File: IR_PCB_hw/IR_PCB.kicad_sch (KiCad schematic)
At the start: 130 parts, among them Q1 M28S, Q10 SI2301, Q11 SI2301, Q2 M28S, Q3 TSOP4856, Q4 TSOP4856, Q5 SI2301, Q6 TSOP4856, Q7 SI2301, Q8 SI2301, Q9 SI2301

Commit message: Replace USB conn with micro one Replace 0402 wit 0603
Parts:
- removed R2, R3: 5k1, Resistors:RES_0402_Fab, symbol Tittar_kl:R
- removed XL4: USB_C 24PF-009, Connectors:USBC_24PF-009, symbol Connectors_kl:USB_C
- added XL4: DS1105-11, Connectors:USBmicro_Connfly_DS1105-11, symbol Connectors_kl:USB_MICRO_3H
- C10: footprint Capacitors:CAP_0603_Fab -> Capacitors:CAP_0603_Silks
- C11: renamed from C12; footprint Capacitors:CAP_0402_Fab -> Capacitors:CAP_0603_Silks
- C12: renamed from C13; footprint Capacitors:CAP_0402_Fab -> Capacitors:CAP_0603_Silks
- C13: renamed from C14; footprint Capacitors:CAP_0402_Fab -> Capacitors:CAP_0603_Silks
- C14: renamed from C11; footprint Capacitors:CAP_0402_Fab -> Capacitors:CAP_0603_Silks
- C15: renamed from C16; footprint Capacitors:CAP_0402_Fab -> Capacitors:CAP_0603_Silks
- C17: renamed from C18; footprint Capacitors:CAP_0402_Fab -> Capacitors:CAP_0603_Silks
- C19: renamed from C20; footprint Capacitors:CAP_0402_Fab -> Capacitors:CAP_0603_Silks
- C2, C3, C4, C5, C6, C7, C8, C9: footprint Capacitors:CAP_0402_Fab -> Capacitors:CAP_0603_Silks
- C21: renamed from C22; footprint Capacitors:CAP_0402_Fab -> Capacitors:CAP_0603_Silks
- C22: renamed from C23; footprint Capacitors:CAP_0603_Fab -> Capacitors:CAP_0603_Silks
- C23: renamed from C24; footprint Capacitors:CAP_0402_Fab -> Capacitors:CAP_0603_Silks
- C24: renamed from C25; footprint Capacitors:CAP_0603_Fab -> Capacitors:CAP_0603_Silks
- C25: renamed from C26; footprint Capacitors:CAP_0603_Fab -> Capacitors:CAP_0603_Silks
- D9: renamed from D13; Price 10.59 -> 10.35
- R1: footprint Resistors:RES_0402_Fab -> Resistors:RES_0603_Silks
- R10: renamed from R12; footprint Resistors:RES_0402_Fab -> Resistors:RES_0603_Silks
- R11: renamed from R13; footprint Resistors:RES_0402_Fab -> Resistors:RES_0603_Silks
- R12: renamed from R14; footprint Resistors:RES_0402_Fab -> Resistors:RES_0603_Silks
- R13: renamed from R15; footprint Resistors:RES_0402_Fab -> Resistors:RES_0603_Silks
- R14: renamed from R16; footprint Resistors:RES_0402_Fab -> Resistors:RES_0603_Silks
- R15: renamed from R17; footprint Resistors:RES_0402_Fab -> Resistors:RES_0603_Silks
- R16: renamed from R18; footprint Resistors:RES_0402_Fab -> Resistors:RES_0603_Silks
- R17: renamed from R19; footprint Resistors:RES_0402_Fab -> Resistors:RES_0603_Silks
- R18: renamed from R20; footprint Resistors:RES_0402_Fab -> Resistors:RES_0603_Silks
- R19: renamed from R21; footprint Resistors:RES_0402_Fab -> Resistors:RES_0603_Silks
- R2: renamed from R4; footprint Resistors:RES_0402_Fab -> Resistors:RES_0603_Silks
- R20: renamed from R22; footprint Resistors:RES_0402_Fab -> Resistors:RES_0603_Silks
- R21: renamed from R23; footprint Resistors:RES_0402_Fab -> Resistors:RES_0603_Silks
- R22: renamed from R24; footprint Resistors:RES_0402_Fab -> Resistors:RES_0603_Silks
- R23: renamed from R29; footprint Resistors:RES_0402_Fab -> Resistors:RES_0603_Silks
- R24: renamed from R25; footprint Resistors:RES_0402_Fab -> Resistors:RES_0603_Silks
- R25: renamed from R26; footprint Resistors:RES_0402_Fab -> Resistors:RES_0603_Silks
- R26: renamed from R27; footprint Resistors:RES_0402_Fab -> Resistors:RES_0603_Silks
- R3: renamed from R5; footprint Resistors:RES_0402_Fab -> Resistors:RES_0603_Silks
- R4: renamed from R6; footprint Resistors:RES_0402_Fab -> Resistors:RES_0603_Silks
- R5: renamed from R7; footprint Resistors:RES_0402_Fab -> Resistors:RES_0603_Silks
- R6: renamed from R8; footprint Resistors:RES_0402_Fab -> Resistors:RES_0603_Silks
- R7: renamed from R9; footprint Resistors:RES_0402_Fab -> Resistors:RES_0603_Silks
- R8: renamed from R10; footprint Resistors:RES_0402_Fab -> Resistors:RES_0603_Silks
- R9: renamed from R11; footprint Resistors:RES_0402_Fab -> Resistors:RES_0603_Silks
- renumbered C17 to C16, C19 to C18, C21 to C20, D9 to D10, D10 to D11, D11 to D12, D12 to D13, Q9 to Q10, Q10 to Q9, TP2 to TP1, TP3 to TP2, TP4 to TP3, TP5 to TP4, XL14 to XL10, XL15 to XL11, XL16 to XL12, XL17 to XL13, XL18 to XL14, XL19 to XL15, XL20 to XL16, XL21 to XL17, XL22 to XL18, XL23 to XL19, XL24 to XL20, XL7 to XL6, XL8 to XL7, XL9 to XL8, XL10 to XL9
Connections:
- net +5vUSB: now also XL4.1 (UVcc)
- net GND: now also XL4.4 (UID), XL4.5 (UGND)
- net USB_D+: now also XL4.3 (D+)
- net USB_D-: now also XL4.2 (D-)
- no-connect marks 18 -> 7

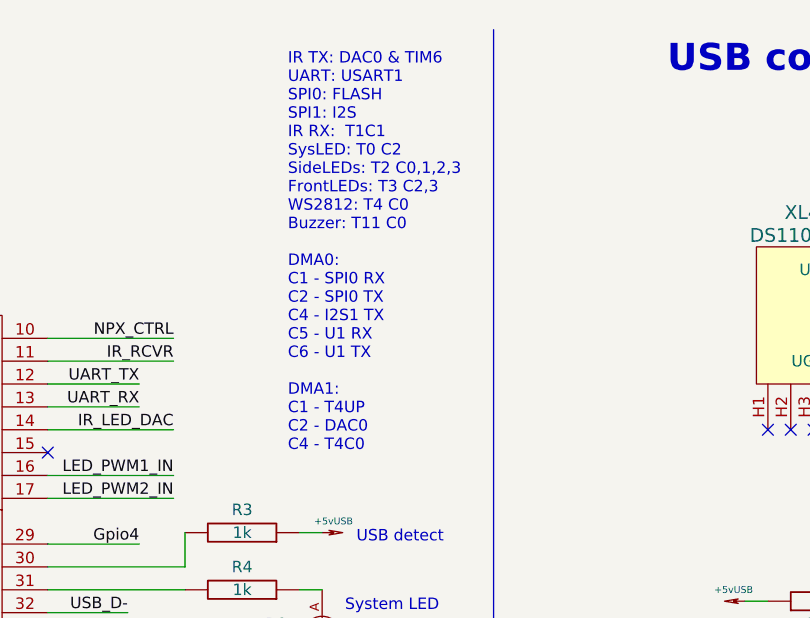
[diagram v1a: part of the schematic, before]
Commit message: Switching to CDC+MSD
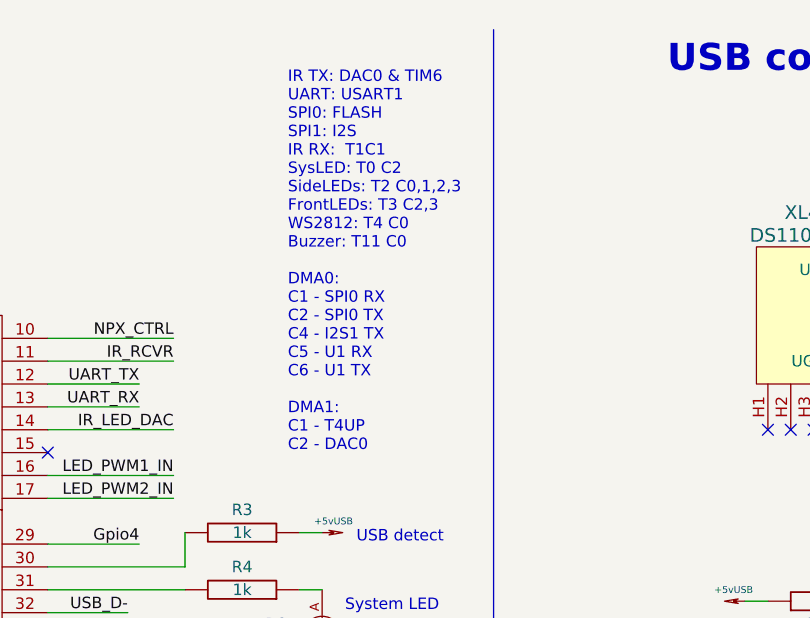
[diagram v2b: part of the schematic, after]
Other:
- note added: "IR TX: DAC0 & TIM6 UART: USART1 SPI0: FLASH SPI1: I2S IR RX: T1C1 SysLED: T0 C2 SideLEDs: T2 C0,1,2,3 FrontLEDs: T3 C2,3 WS2812: T4 C0 Buzzer: T11 C0 DMA0: C1 - SPI0 RX C2 - SPI0 TX C4 - I2S1 TX C5 - U1 RX C6 - U1 TX DMA1: C1 - T4UP C2 - DAC0"
- note removed: "IR TX: DAC0 & TIM6 UART: USART1 SPI0: FLASH SPI1: I2S IR RX: T1C1 SysLED: T0 C2 SideLEDs: T2 C0,1,2,3 FrontLEDs: T3 C2,3 WS2812: T4 C0 Buzzer: T11 C0 DMA0: C1 - SPI0 RX C2 - SPI0 TX C4 - I2S1 TX C5 - U1 RX C6 - U1 TX DMA1: C1 - T4UP C2 - DAC0 C4 - T4C0"
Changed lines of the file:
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@@
     (effects (font (size 1.27 1.27) bold) (justify left bottom))
   )
-  (text "IR TX: DAC0 & TIM6\nUART: USART1\nSPI0: FLASH\nSPI1: I2S\nIR RX:  T1C1\nSysLED: T0 C2\nSideLEDs: T2 C0,1,2,3\nFrontLEDs: T3 C2,3\nWS2812: T4 C0\nBuzzer: T11 C0\n\nDMA0:\nC1 - SPI0 RX\nC2 - SPI0 TX\nC4 - I2S1 TX\nC5 - U1 RX\nC6 - U1 TX\n\nDMA1:\nC1 - T4UP\nC2 - DAC0\nC4 - T4C0"
+  (text "IR TX: DAC0 & TIM6\nUART: USART1\nSPI0: FLASH\nSPI1: I2S\nIR RX:  T1C1\nSysLED: T0 C2\nSideLEDs: T2 C0,1,2,3\nFrontLEDs: T3 C2,3\nWS2812: T4 C0\nBuzzer: T11 C0\n\nDMA0:\nC1 - SPI0 RX\nC2 - SPI0 TX\nC4 - I2S1 TX\nC5 - U1 RX\nC6 - U1 TX\n\nDMA1:\nC1 - T4UP\nC2 - DAC0"
     (at 167.64 60.96 0)
     (effects (font (size 1.27 1.27)) (justify left bottom))

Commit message: Preparation for factory
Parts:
- BZ1, D1, D10, D11, D12, D13, D3, D4, D5, D6, D7, D8, Q3, Q4, Q6: Comment (none) -> DoNotMount
- C10: PN CL10A106MP8NNNC -> CL10A106MQ8NNNC; URL https://www.promelec.ru/product/335887/ -> https://www.promelec.ru/product/334535/; Voltage 10v -> 6V3
- C2: PN CC0402KRX7R7BB104 -> CC0603KRX7R9BB104; Price 0.17 -> 0.34; URL https://www.promelec.ru/product/141827/ -> https://www.promelec.ru/product/126354/; Voltage 16V -> 50V
- C3: Manufacturer Murata -> Samsung; PN GRM155R61A225KE95D -> CL10A225KO8NNNC; URL https://www.promelec.ru/product/315859/ -> https://www.promelec.ru/product/316243/; Voltage 10V -> 16V
- C4: PN CC0402JRNPO9BN180 -> CC0603JRNPO9BN180; URL https://www.promelec.ru/product/188454/ -> https://www.promelec.ru/product/128216/
- C6: Manufacturer Hottech -> Samsung; PN C1005A105K100NT -> CL10A105KO8NNNC; URL https://www.promelec.ru/product/522035/ -> https://www.promelec.ru/product/335757/; Voltage 10V -> 16V
- R1: PN RC0402FR-0710KL -> RC0603FR-0710KL; URL https://www.promelec.ru/product/305624/ -> https://www.promelec.ru/product/108599/
- R2: PN RI0402L1001FT -> RC0603FR-071KL; URL https://www.promelec.ru/product/415937/ -> https://www.promelec.ru/product/22771/
- R5: PN RI0402L2R00FT -> RC0603FR-072RL; URL https://www.promelec.ru/product/529480/ -> https://www.promelec.ru/product/59444/
- R6: PN RC0402FR-07100RL -> RC0603FR-07100RL; URL https://www.promelec.ru/product/229700/ -> https://www.promelec.ru/product/57782/
- R9: PN RC0402FR-0751RL -> RC0603FR-0751RL; URL https://www.promelec.ru/product/305769/ -> https://www.promelec.ru/product/18324/
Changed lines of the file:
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@@
       (effects (font (size 2.0066 2.0066)) hide)
     )
-    (property "PN" "RC0402FR-0751RL" (at 391.16 142.24 0)
+    (property "PN" "RC0603FR-0751RL" (at 391.16 142.24 0)
       (effects (font (size 1.27 1.27)) hide)
     )
@@
       (effects (font (size 1.27 1.27)) hide)
     )
-    (property "URL" "https://www.promelec.ru/product/305769/" (at 391.16 142.24 90)
+    (property "URL" "https://www.promelec.ru/product/18324/" (at 391.16 142.24 90)
       (effects (font (size 1.27 1.27)) hide)
     )
@@
       (effects (font (size 1.27 1.27)) hide)
     )
+    (property "Comment" "DoNotMount" (at 389.89 34.29 90)
+      (effects (font (size 1.27 1.27)) hide)
+    )
     (pin "A")
     (pin "C")
@@
       (effects (font (size 1.27 1.27)) hide)
     )
-    (property "PN" "C1005A105K100NT" (at 245.11 118.11 0)
+    (property "PN" "CL10A105KO8NNNC" (at 245.11 118.11 0)
       (effects (font (size 1.27 1.27)) hide)
     )
-    (property "Manufacturer" "Hottech" (at 245.11 118.11 0)
+    (property "Manufacturer" "Samsung" (at 245.11 118.11 0)
       (effects (font (size 1.27 1.27)) hide)
     )
@@
       (effects (font (size 1.27 1.27)) hide)
     )
-    (property "Voltage" "10V" (at 245.11 118.11 0)
+    (property "Voltage" "16V" (at 245.11 118.11 0)
       (effects (font (size 1.27 1.27)) (justify left))
     )
-    (property "URL" "https://www.promelec.ru/product/522035/" (at 245.11 118.11 0)
+    (property "URL" "https://www.promelec.ru/product/335757/" (at 245.11 118.11 0)
       (effects (font (size 1.27 1.27)) hide)
     )
@@
       (effects (font (size 1.27 1.27)) hide)
     )
+    (property "Comment" "DoNotMount" (at 400.05 85.09 90)
+      (effects (font (size 1.27 1.27)) hide)
+    )
     (pin "A")
     (pin "C")
@@
       (effects (font (size 1.27 1.27)) hide)
     )
+    (property "Comment" "DoNotMount" (at 316.23 153.67 0)
+      (effects (font (size 1.27 1.27)) hide)
+    )
     (pin "1")
     (pin "2")
@@
       (effects (font (size 1.27 1.27)) hide)
     )
+    (property "Comment" "DoNotMount" (at 238.76 254 0)
+      (effects (font (size 1.27 1.27)) hide)
+    )
     (pin "A")
     (pin "C")
@@
       (effects (font (size 1.27 1.27)) hide)
     )
+    (property "Comment" "DoNotMount" (at 238.76 226.06 0)
+      (effects (font (size 1.27 1.27)) hide)
+    )
     (pin "A")
     (pin "C")
@@
       (effects (font (size 1.27 1.27)) hide)
     )
+    (property "Comment" "DoNotMount" (at 238.76 262.89 0)
+      (effects (font (size 1.27 1.27)) hide)
+    )
     (pin "A")
     (pin "C")
@@
       (effects (font (size 1.27 1.27)) hide)
     )
+    (property "Comment" "DoNotMount" (at 397.51 236.22 0)
+      (effects (font (size 1.27 1.27)) hide)
+    )
     (pin "1")
     (pin "2")
@@
       (effects (font (size 2.0066 2.0066)) hide)
     )
-    (property "PN" "RC0402FR-07100RL" (at 393.7 77.47 0)
+    (property "PN" "RC0603FR-07100RL" (at 393.7 77.47 0)
       (effects (font (size 1.27 1.27)) hide)
     )
@@
       (effects (font (size 1.27 1.27)) hide)
     )
-    (property "URL" "https://www.promelec.ru/product/229700/" (at 393.7 77.47 90)
+    (property "URL" "https://www.promelec.ru/product/57782/" (at 393.7 77.47 90)
       (effects (font (size 1.27 1.27)) hide)
     )
@@
       (effects (font (size 1.27 1.27)) hide)
     )
-    (property "PN" "GRM155R61A225KE95D" (at 238.76 77.47 0)
+    (property "PN" "CL10A225KO8NNNC" (at 238.76 77.47 0)
       (effects (font (size 1.27 1.27)) hide)
     )
-    (property "Manufacturer" "Murata" (at 238.76 77.47 0)
+    (property "Manufacturer" "Samsung" (at 238.76 77.47 0)
       (effects (font (size 1.27 1.27)) hide)
     )
@@
       (effects (font (size 1.27 1.27)) hide)
     )
-    (property "Voltage" "10V" (at 238.76 78.74 0)
+    (property "Voltage" "16V" (at 238.76 78.74 0)
       (effects (font (size 0.7 0.7)) (justify left))
     )
-    (property "URL" "https://www.promelec.ru/product/315859/" (at 238.76 77.47 90)
+    (property "URL" "https://www.promelec.ru/product/316243/" (at 238.76 77.47 90)
       (effects (font (size 1.27 1.27)) hide)
     )
@@
       (effects (font (size 1.27 1.27)) hide)
     )
+    (property "Comment" "DoNotMount" (at 238.76 234.95 0)
+      (effects (font (size 1.27 1.27)) hide)
+    )
     (pin "A")
     (pin "C")
@@
       (effects (font (size 1.27 1.27)) hide)
     )
+    (property "Comment" "DoNotMount" (at 364.49 138.43 0)
+      (effects (font (size 1.27 1.27)) hide)
+    )
     (pin "1")
     (pin "2")
@@
       (effects (font (size 2.0066 2.0066)) hide)
     )
-    (property "PN" "RI0402L1001FT" (at 326.39 64.77 0)
+    (property "PN" "RC0603FR-071KL" (at 326.39 64.77 0)
       (effects (font (size 1.27 1.27)) hide)
     )
@@
       (effects (font (size 1.27 1.27)) hide)
     )
-    (property "URL" "https://www.promelec.ru/product/415937/" (at 326.39 64.77 0)
+    (property "URL" "https://www.promelec.ru/product/22771/" (at 326.39 64.77 0)
       (effects (font (size 1.27 1.27)) hide)
     )
@@
       (effects (font (size 2.0066 2.0066)) hide)
     )
-    (property "PN" "RC0402FR-0710KL" (at 300.99 48.26 0)
+    (property "PN" "RC0603FR-0710KL" (at 300.99 48.26 0)
       (effects (font (size 1.27 1.27)) hide)
     )
@@
       (effects (font (size 1.27 1.27)) hide)
     )
-    (property "URL" "https://www.promelec.ru/product/305624/" (at 300.99 48.26 90)
+    (property "URL" "https://www.promelec.ru/product/108599/" (at 300.99 48.26 90)
       (effects (font (size 1.27 1.27)) hide)
     )
@@
       (effects (font (size 1.27 1.27)) hide)
     )
-    (property "PN" "CC0402JRNPO9BN180" (at 175.26 109.22 0)
+    (property "PN" "CC0603JRNPO9BN180" (at 175.26 109.22 0)
       (effects (font (size 1.27 1.27)) hide)
     )
@@
       (effects (font (size 1.27 1.27)) (justify left) hide)
     )
-    (property "URL" "https://www.promelec.ru/product/188454/" (at 175.26 109.22 90)
+    (property "URL" "https://www.promelec.ru/product/128216/" (at 175.26 109.22 90)
       (effects (font (size 1.27 1.27)) hide)
     )
@@
       (effects (font (size 1.524 1.524)) hide)
     )
-    (property "Price" "0.17" (at 317.5 34.29 0)
+    (property "Price" "0.34" (at 317.5 34.29 0)
       (effects (font (size 1.524 1.524)) hide)
     )
@@
       (effects (font (size 1.27 1.27)) hide)
     )
-    (property "PN" "CC0402KRX7R7BB104" (at 317.5 34.29 0)
+    (property "PN" "CC0603KRX7R9BB104" (at 317.5 34.29 0)
       (effects (font (size 1.27 1.27)) hide)
     )
@@
       (effects (font (size 1.27 1.27)) hide)
     )
-    (property "Voltage" "16V" (at 317.5 34.29 0)
+    (property "Voltage" "50V" (at 317.5 34.29 0)
       (effects (font (size 1.27 1.27)) (justify left))
     )
-    (property "URL" "https://www.promelec.ru/product/141827/" (at 317.5 34.29 0)
+    (property "URL" "https://www.promelec.ru/product/126354/" (at 317.5 34.29 0)
       (effects (font (size 1.27 1.27)) hide)
     )
@@
       (effects (font (size 1.27 1.27)) hide)
     )
+    (property "Comment" "DoNotMount" (at 238.76 189.23 0)
+      (effects (font (size 1.27 1.27)) hide)
+    )
     (pin "A")
     (pin "C")
@@
       (effects (font (size 1.27 1.27)) hide)
     )
+    (property "Comment" "DoNotMount" (at 238.76 198.12 0)
+      (effects (font (size 1.27 1.27)) hide)
+    )
     (pin "A")
     (pin "C")
@@
       (effects (font (size 1.27 1.27)) hide)
     )
+    (property "Comment" "DoNotMount" (at 364.49 166.37 0)
+      (effects (font (size 1.27 1.27)) hide)
+    )
     (pin "1")
     (pin "2")
@@
       (effects (font (size 1.27 1.27)) hide)
     )
+    (property "Comment" "DoNotMount" (at 238.76 161.29 0)
+      (effects (font (size 1.27 1.27)) hide)
+    )
     (pin "A")
     (pin "C")
@@
       (effects (font (size 1.27 1.27)) hide)
     )
+    (property "Comment" "DoNotMount" (at 238.76 170.18 0)
+      (effects (font (size 1.27 1.27)) hide)
+    )
     (pin "A")
     (pin "C")
@@
       (effects (font (size 1.27 1.27)) hide)
     )
-    (property "PN" "CL10A106MP8NNNC" (at 53.34 121.92 0)
+    (property "PN" "CL10A106MQ8NNNC" (at 53.34 121.92 0)
       (effects (font (size 1.27 1.27)) hide)
     )
@@
       (effects (font (size 1.27 1.27)) hide)
     )
-    (property "Voltage" "10v" (at 53.34 121.92 0)
+    (property "Voltage" "6V3" (at 53.34 121.92 0)
       (effects (font (size 1.27 1.27)) (justify left))
     )
-    (property "URL" "https://www.promelec.ru/product/335887/" (at 53.34 121.92 0)
+    (property "URL" "https://www.promelec.ru/product/334535/" (at 53.34 121.92 0)
       (effects (font (size 1.27 1.27)) hide)
     )
@@
       (effects (font (size 2.0066 2.0066)) hide)
     )
-    (property "PN" "RI0402L2R00FT" (at 227.33 77.47 0)
+    (property "PN" "RC0603FR-072RL" (at 227.33 77.47 0)
       (effects (font (size 1.27 1.27)) hide)
     )
@@
       (effects (font (size 1.27 1.27)) hide)
     )
-    (property "URL" "https://www.promelec.ru/product/529480/" (at 227.33 77.47 90)
+    (property "URL" "https://www.promelec.ru/product/59444/" (at 227.33 77.47 90)
       (effects (font (size 1.27 1.27)) hide)
     )
@@
       (effects (font (size 1.27 1.27)) hide)
     )
+    (property "Comment" "DoNotMount" (at 400.05 109.22 90)
+      (effects (font (size 1.27 1.27)) hide)
+    )

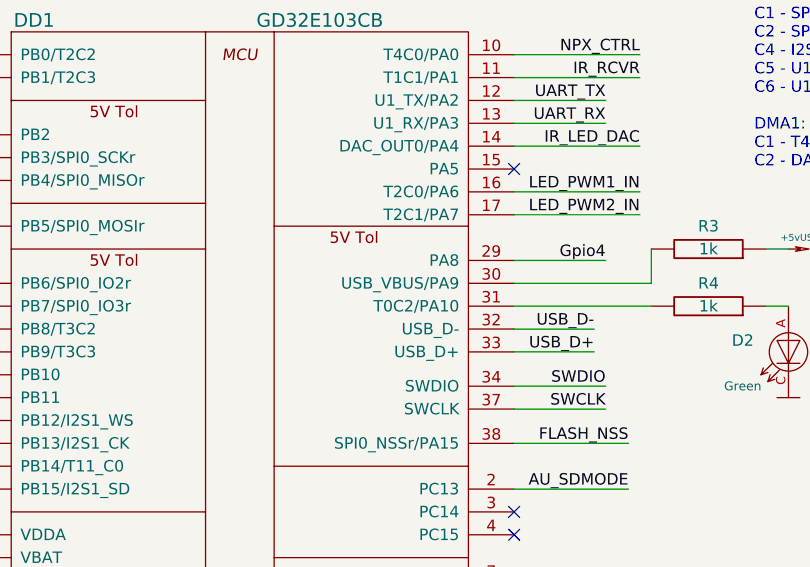
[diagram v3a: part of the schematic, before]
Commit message: Huge refactoring + PWM input works
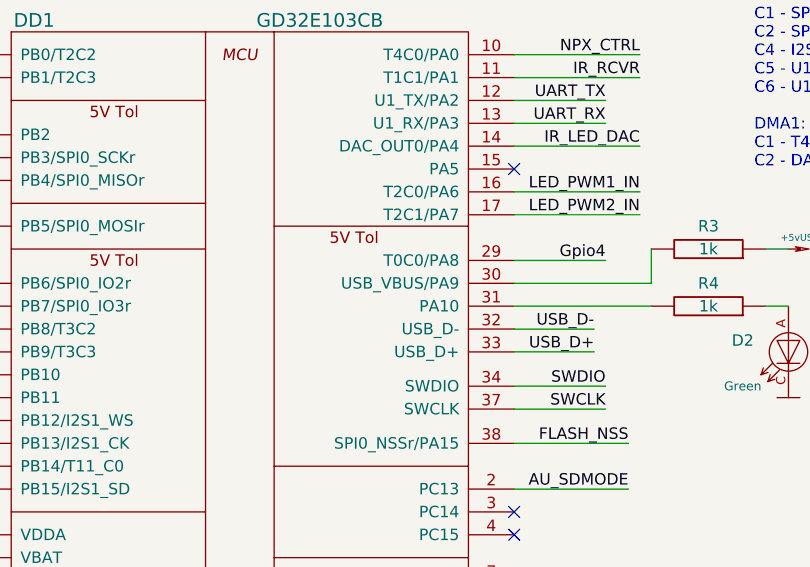
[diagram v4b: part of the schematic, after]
